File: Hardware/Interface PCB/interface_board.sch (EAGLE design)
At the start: 13 parts

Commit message: Interface board
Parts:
- removed D1: PURPLE, SparkFun-LED:LED-PURPLE1206
- removed PRGM: SWITCH-MOMENTARY-2SMD-REDUNDANT, SparkFun-Electromechanical:SWITCH-MOMENTARY-2SMD-REDUNDANT
- added JP2, JP4: (no value), pinhead:PINHD-1X3
- added JP3: (no value), pinhead:PINHD-2X4
- added PWR: PURPLE, SparkFun-LED:LED-PURPLE1206
- added R10, R11, R3, R4, R5, R6, R7, R8, R9: 10k, rcl:R-US_R1206
- added S1: PRGM, switch-dil:SD4-01
- added SJ1, SJ2, SJ3, SJ4: (no value), jumper:SJ
- added U1, U2, U3, U4: BSS138-7-F, bss138_sot_23:BSS138-7-F
- C1: device rcl:CPOL-US153CLV-0605 -> rcl:CPOL-USE2-5
- C3: value 680-1000uF -> 680uF
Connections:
- net N$1 renamed ADC
- net N$10 renamed GPIO15
- net N$12 renamed RESET
- net N$5 renamed GPIO4
- net N$8 renamed GPIO13
- removed net N$11: JP1.16, U$1.GPIO16
- removed net N$3: JP1.4, PRGM.1, U$1.GPIO0
- removed net N$4: JP1.5, U$1.GPIO2
- removed net N$9: JP1.14, U$1.GPIO14
- new net CH_PD: JP3.6, U$1.CH_PD
- new net GPIO0: JP1.4, JP3.3, R3.1, S1.2, U$1.GPIO0
- new net GPIO12: JP1.11, U$1.GPIO12
- new net GPIO14: JP1.14, R9.1, U$1.GPIO14, U4.S
- new net GPIO16: JP1.16, JP3.4, U$1.GPIO16
- new net GPIO2: JP1.5, JP3.5, R8.1, U$1.GPIO2, U3.S
- new net GPIO5: JP1.8, U$1.GPIO5
- new net RX: JP3.1, R5.1, SJ3.1, U$1.RX, U2.S
- new net RX_EXT: R7.1, SJ4.1, U2.D
- new net SCL: R11.1, U4.D
- new net SDA: R10.1, U3.D
- new net TX: JP3.8, R4.1, SJ1.2, U$1.TX, U1.S
- new net TX_EXT: R6.1, SJ2.2, U1.D
- net +3V3: now also JP3.2, JP4.3, R3.2, R4.2, R5.2, R8.2, R9.2, U1.G, U2.G, U3.G, U4.G
- net +5V: now also JP4.2, R10.2, R11.2, R6.2, R7.2
- net GND: now also JP2.1, JP3.7, JP4.1, PWR.C; no longer D1.C, PRGM.2
- net N$2: now also PWR.A; no longer D1.A
- net N$6: now also JP2.3, SJ1.1, SJ2.1; no longer JP1.11, U$1.GPIO5
- net N$7: now also JP2.2, SJ3.2, SJ4.2; no longer JP1.8, U$1.GPIO12
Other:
- note added: "External reset headers? CH_PD headers? MOSFET to ground for TTL logic compatability? Level converter on RX/TX lines. bi-directional level converters on I2C GPIO lines?"
- moved on the sheet: C1, C2, C3, C4, C5, JP1, NCP1117-3.3V, R1, R2, RESET, U$1

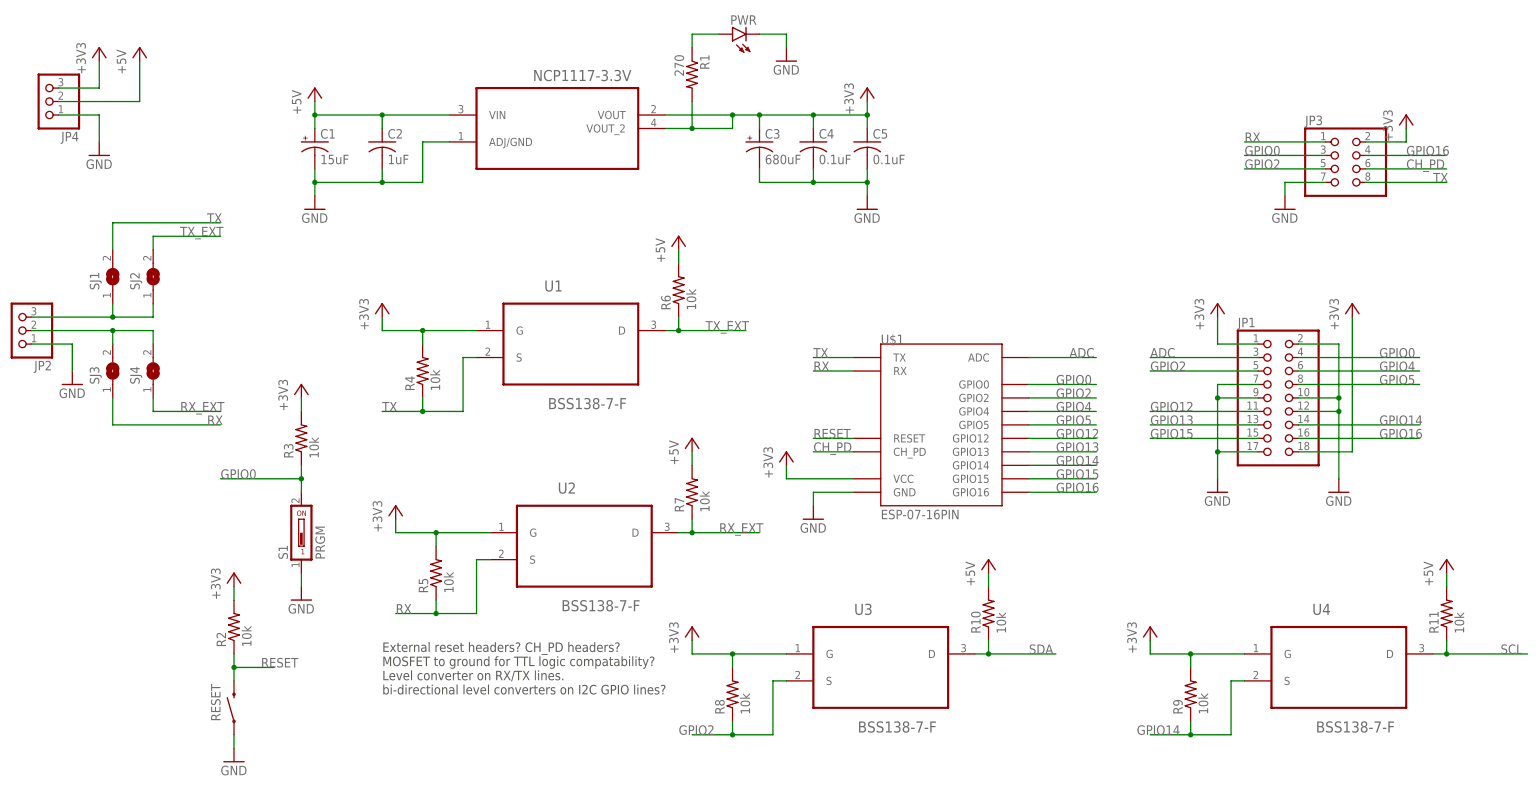
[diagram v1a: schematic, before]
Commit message: Main program
Added config file parser using ConfigParse, command-line parser using
argparse, logging, and signal handling. Finished UDP service discovery
process.
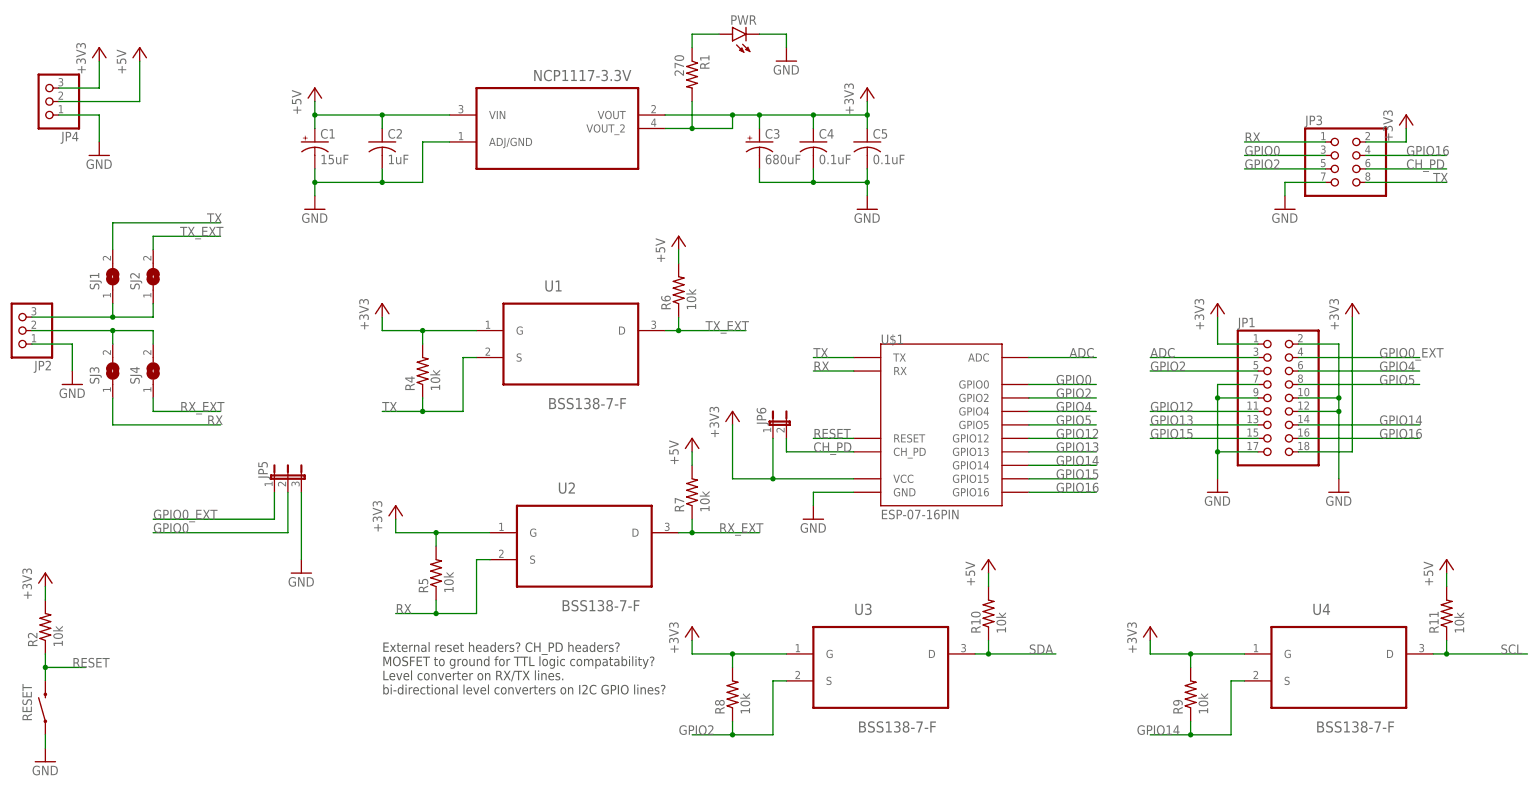
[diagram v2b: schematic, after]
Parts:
- removed R3: 10k, rcl:R-US_R1206
- removed S1: PRGM, switch-dil:SD4-01
- added JP5: (no value), jumper:JP2E
- added JP6: (no value), jumper:JP1E
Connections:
- new net GPIO0_EXT: JP1.4, JP5.1
- net +3V3: now also JP6.1; no longer R3.2
- net CH_PD: now also JP6.2
- net GND: now also JP5.3
- net GPIO0: now also JP5.2; no longer JP1.4, R3.1, S1.2
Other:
- moved on the sheet: R2, RESET
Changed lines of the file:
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@@
 <part name="GND10" library="supply1" deviceset="GND" device=""/>
 <part name="+3V7" library="supply1" deviceset="+3V3" device=""/>
-<part name="R3" library="rcl" deviceset="R-US_" device="R1206" value="10k"/>
-<part name="+3V8" library="supply1" deviceset="+3V3" device=""/>
 <part name="U1" library="bss138_sot_23" deviceset="BSS138-7-F" device=""/>
 <part name="U2" library="bss138_sot_23" deviceset="BSS138-7-F" device=""/>
@@
 <part name="JP2" library="pinhead" deviceset="PINHD-1X3" device=""/>
 <part name="GND9" library="supply1" deviceset="GND" device=""/>
-<part name="S1" library="switch-dil" deviceset="SD4-01" device="" value="PRGM"/>
 <part name="SJ1" library="jumper" deviceset="SJ" device=""/>
 <part name="SJ2" library="jumper" deviceset="SJ" device=""/>
@@
 <part name="P+5" library="supply1" deviceset="+5V" device=""/>
 <part name="P+6" library="supply1" deviceset="+5V" device=""/>
+<part name="JP5" library="jumper" deviceset="JP2E" device=""/>
+<part name="JP6" library="jumper" deviceset="JP1E" device=""/>
 </parts>
 <sheets>
@@
 <instance part="GND3" gate="1" x="55.88" y="109.22"/>
 <instance part="GND4" gate="1" x="60.96" y="22.86"/>
-<instance part="+3V2" gate="G$1" x="55.88" y="35.56"/>
+<instance part="+3V2" gate="G$1" x="45.72" y="43.18"/>
 <instance part="JP1" gate="A" x="147.32" y="45.72"/>
 <instance part="GND5" gate="1" x="137.16" y="27.94"/>
@@
 <instance part="+3V3" gate="G$1" x="137.16" y="63.5"/>
 <instance part="+3V4" gate="G$1" x="162.56" y="63.5"/>
-<instance part="RESET" gate="G$1" x="-48.26" y="-12.7" smashed="yes" rot="R90">
-<attribute name="NAME" x="-50.8" y="-15.24" size="1.778" layer="95" rot="R90"/>
+<instance part="RESET" gate="G$1" x="-83.82" y="-12.7" smashed="yes" rot="R90">
+<attribute name="NAME" x="-86.36" y="-15.24" size="1.778" layer="95" rot="R90"/>
 </instance>
-<instance part="GND7" gate="1" x="-48.26" y="-22.86"/>
-<instance part="+3V5" gate="G$1" x="-48.26" y="12.7"/>
-<instance part="R2" gate="G$1" x="-48.26" y="2.54" rot="R90"/>
-<instance part="GND8" gate="1" x="-35.56" y="7.62"/>
+<instance part="GND7" gate="1" x="-83.82" y="-22.86"/>
+<instance part="+3V5" gate="G$1" x="-83.82" y="12.7"/>
+<instance part="R2" gate="G$1" x="-83.82" y="2.54" rot="R90"/>
+<instance part="GND8" gate="1" x="-35.56" y="12.7"/>
 <instance part="JP3" gate="A" x="160.02" y="88.9"/>
 <instance part="GND10" gate="1" x="149.86" y="81.28"/>
 <instance part="+3V7" gate="G$1" x="172.72" y="99.06"/>
-<instance part="R3" gate="G$1" x="-35.56" y="38.1" rot="R90"/>
-<instance part="+3V8" gate="G$1" x="-35.56" y="48.26"/>
 <instance part="U1" gate="A" x="15.24" y="58.42"/>
 <instance part="U2" gate="A" x="17.78" y="20.32"/>
@@
 <instance part="JP2" gate="A" x="-88.9" y="58.42" rot="R180"/>
 <instance part="GND9" gate="1" x="-78.74" y="48.26"/>
-<instance part="S1" gate="1" x="-35.56" y="20.32"/>
 <instance part="SJ1" gate="1" x="-71.12" y="68.58" rot="R90"/>
 <instance part="SJ2" gate="1" x="-63.5" y="68.58" rot="R90"/>
@@
 <instance part="P+5" gate="1" x="93.98" y="15.24"/>
 <instance part="P+6" gate="1" x="180.34" y="15.24"/>
+<instance part="JP5" gate="1" x="-38.1" y="30.48"/>
+<instance part="JP6" gate="A" x="53.34" y="40.64"/>
 </instances>
 <busses>
@@
 <pinref part="GND7" gate="1" pin="GND"/>
 <pinref part="RESET" gate="G$1" pin="1"/>
-<wire x1="-48.26" y1="-20.32" x2="-48.26" y2="-17.78" width="0.1524" layer="91"/>
-</segment>
-<segment>
-<wire x1="-35.56" y1="12.7" x2="-35.56" y2="10.16" width="0.1524" layer="91"/>
-<pinref part="GND8" gate="1" pin="GND"/>
+<wire x1="-83.82" y1="-20.32" x2="-83.82" y2="-17.78" width="0.1524" layer="91"/>
 </segment>
 <segment>
@@
 <wire x1="-73.66" y1="99.06" x2="-73.66" y2="93.98" width="0.1524" layer="91"/>
 <pinref part="GND11" gate="1" pin="GND"/>
+</segment>
+<segment>
+<pinref part="GND8" gate="1" pin="GND"/>
+<pinref part="JP5" gate="1" pin="3"/>
+<wire x1="-35.56" y1="15.24" x2="-35.56" y2="27.94" width="0.1524" layer="91"/>
 </segment>
 </net>
@@
 <pinref part="U$1" gate="G$1" pin="VCC"/>
 <pinref part="+3V2" gate="G$1" pin="+3V3"/>
-<wire x1="68.58" y1="30.48" x2="55.88" y2="30.48" width="0.1524" layer="91"/>
-<wire x1="55.88" y1="30.48" x2="55.88" y2="33.02" width="0.1524" layer="91"/>
+<wire x1="68.58" y1="30.48" x2="53.34" y2="30.48" width="0.1524" layer="91"/>
+<wire x1="53.34" y1="30.48" x2="45.72" y2="30.48" width="0.1524" layer="91"/>
+<wire x1="45.72" y1="30.48" x2="45.72" y2="40.64" width="0.1524" layer="91"/>
+<pinref part="JP6" gate="A" pin="1"/>
+<wire x1="53.34" y1="38.1" x2="53.34" y2="30.48" width="0.1524" layer="91"/>
+<junction x="53.34" y="30.48"/>
 </segment>
 <segment>
@@
 <pinref part="+3V5" gate="G$1" pin="+3V3"/>
 <pinref part="R2" gate="G$1" pin="2"/>
-<wire x1="-48.26" y1="10.16" x2="-48.26" y2="7.62" width="0.1524" layer="91"/>
+<wire x1="-83.82" y1="10.16" x2="-83.82" y2="7.62" width="0.1524" layer="91"/>
 </segment>
 <segment>
@@
 <wire x1="165.1" y1="93.98" x2="172.72" y2="93.98" width="0.1524" layer="91"/>
 <wire x1="172.72" y1="93.98" x2="172.72" y2="96.52" width="0.1524" layer="91"/>
-</segment>
-<segment>
-<pinref part="R3" gate="G$1" pin="2"/>
-<pinref part="+3V8" gate="G$1" pin="+3V3"/>
-<wire x1="-35.56" y1="43.18" x2="-35.56" y2="45.72" width="0.1524" layer="91"/>
 </segment>
 <segment>
@@
 <pinref part="RESET" gate="G$1" pin="2"/>
 <pinref part="R2" gate="G$1" pin="1"/>
-<wire x1="-48.26" y1="-2.54" x2="-48.26" y2="-5.08" width="0.1524" layer="91"/>
-<wire x1="-48.26" y1="-5.08" x2="-48.26" y2="-7.62" width="0.1524" layer="91"/>
-<wire x1="-48.26" y1="-5.08" x2="-40.64" y2="-5.08" width="0.1524" layer="91"/>
-<junction x="-48.26" y="-5.08"/>
-<label x="-43.18" y="-5.08" size="1.778" layer="95"/>
+<wire x1="-83.82" y1="-2.54" x2="-83.82" y2="-5.08" width="0.1524" layer="91"/>
+<wire x1="-83.82" y1="-5.08" x2="-83.82" y2="-7.62" width="0.1524" layer="91"/>
+<wire x1="-83.82" y1="-5.08" x2="-76.2" y2="-5.08" width="0.1524" layer="91"/>
+<junction x="-83.82" y="-5.08"/>
+<label x="-78.74" y="-5.08" size="1.778" layer="95"/>
 </segment>
 <segment>
@@
 <segment>
 <pinref part="U$1" gate="G$1" pin="CH_PD"/>
-<wire x1="68.58" y1="35.56" x2="60.96" y2="35.56" width="0.1524" layer="91"/>
+<wire x1="68.58" y1="35.56" x2="55.88" y2="35.56" width="0.1524" layer="91"/>
 <label x="60.96" y="35.56" size="1.778" layer="95"/>
+<pinref part="JP6" gate="A" pin="2"/>
+<wire x1="55.88" y1="38.1" x2="55.88" y2="35.56" width="0.1524" layer="91"/>
 </segment>
 <segment>
@@
 </segment>
 <segment>
-<wire x1="-35.56" y1="27.94" x2="-35.56" y2="30.48" width="0.1524" layer="91"/>
-<wire x1="-35.56" y1="30.48" x2="-50.8" y2="30.48" width="0.1524" layer="91"/>
-<label x="-50.8" y="30.48" size="1.778" layer="95"/>
-<pinref part="R3" gate="G$1" pin="1"/>
-<wire x1="-35.56" y1="30.48" x2="-35.56" y2="33.02" width="0.1524" layer="91"/>
-<junction x="-35.56" y="30.48"/>
-<pinref part="S1" gate="1" pin="2"/>
-</segment>
-<segment>
-<pinref part="JP1" gate="A" pin="4"/>
-<wire x1="175.26" y1="53.34" x2="152.4" y2="53.34" width="0.1524" layer="91"/>
-<label x="167.64" y="53.34" size="1.778" layer="95"/>
+<wire x1="-38.1" y1="20.32" x2="-63.5" y2="20.32" width="0.1524" layer="91"/>
+<label x="-63.5" y="20.32" size="1.778" layer="95"/>
+<pinref part="JP5" gate="1" pin="2"/>
+<wire x1="-38.1" y1="20.32" x2="-38.1" y2="27.94" width="0.1524" layer="91"/>
 </segment>
 <segment>
@@
 </segment>
 </net>
+<net name="GPIO0_EXT" class="0">
+<segment>
+<pinref part="JP5" gate="1" pin="1"/>
+<wire x1="-63.5" y1="22.86" x2="-40.64" y2="22.86" width="0.1524" layer="91"/>
+<wire x1="-40.64" y1="22.86" x2="-40.64" y2="27.94" width="0.1524" layer="91"/>
+<label x="-63.5" y="22.86" size="1.778" layer="95"/>
+</segment>
+<segment>
+<pinref part="JP1" gate="A" pin="4"/>
+<wire x1="175.26" y1="53.34" x2="152.4" y2="53.34" width="0.1524" layer="91"/>
+<label x="167.64" y="53.34" size="1.778" layer="95"/>
+</segment>
+</net>
